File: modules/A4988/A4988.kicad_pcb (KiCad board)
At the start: 2 copper layers, 40.6 x 40.6 mm, 19 parts, among them J1 Conn_01x10_Male, J2 Conn_01x10_Male, J3 Conn_01x08_Female, J4 Conn_01x08_Female, J5 Conn_01x04_Male, J6 Conn_01x02_Female, SW1 SW_DIP_x03

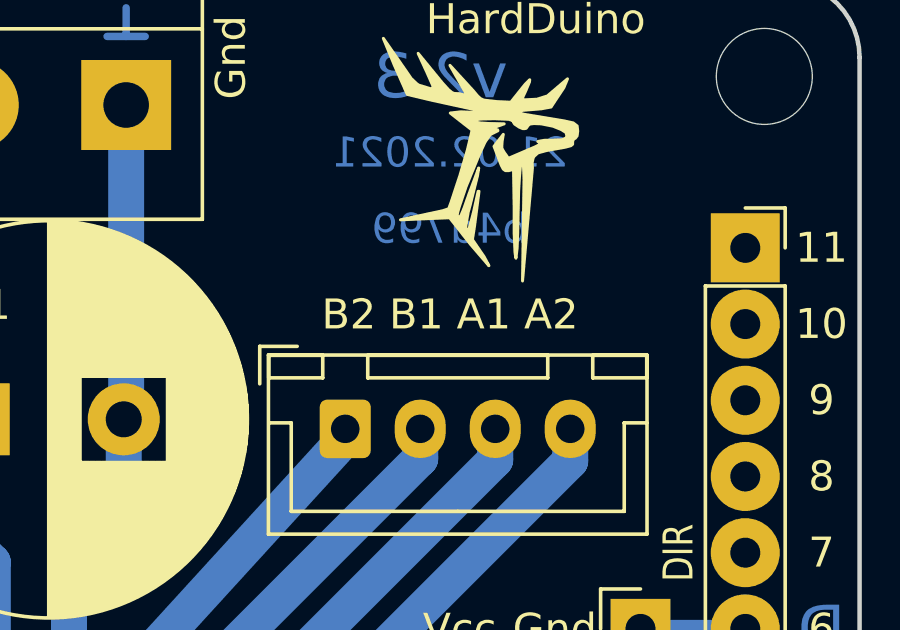
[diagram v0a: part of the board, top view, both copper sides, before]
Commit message: Rename pins. I don't know where I got old names but I found new names on A4988 pcb.
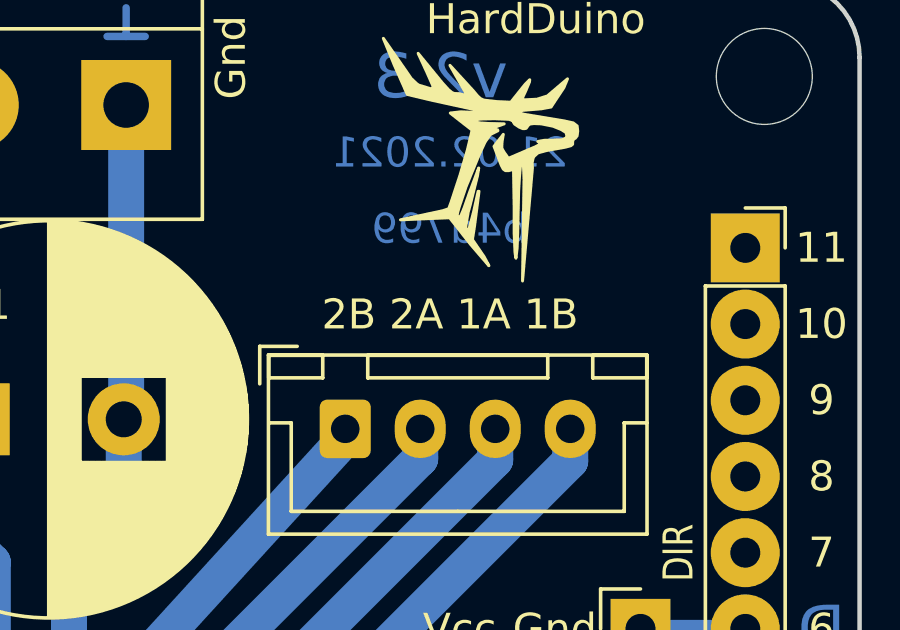
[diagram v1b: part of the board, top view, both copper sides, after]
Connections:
- net /MA1 renamed /1A
- net /MA2 renamed /1B
- net /MB1 renamed /2A
- net /MB2 renamed /2B
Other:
- board text added: "2B 2A 1A 1B"
- board text removed: "B2 B1 A1 A2"

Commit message: Fix hashes
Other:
- board text added: "23.02.2021"
- board text added: "513641"
- board text removed: "21.02.2021"
- board text removed: "b4d799"

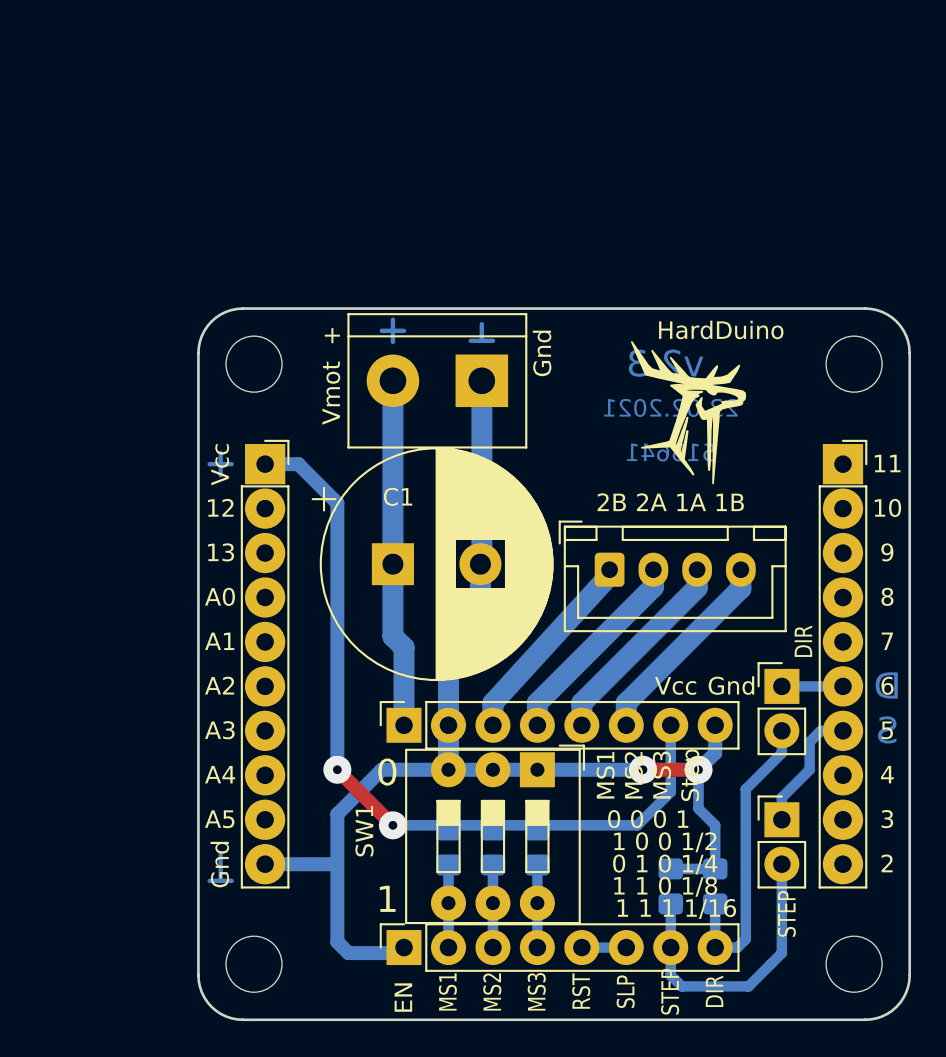
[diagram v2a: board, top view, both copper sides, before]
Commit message: Move mounting holes closer
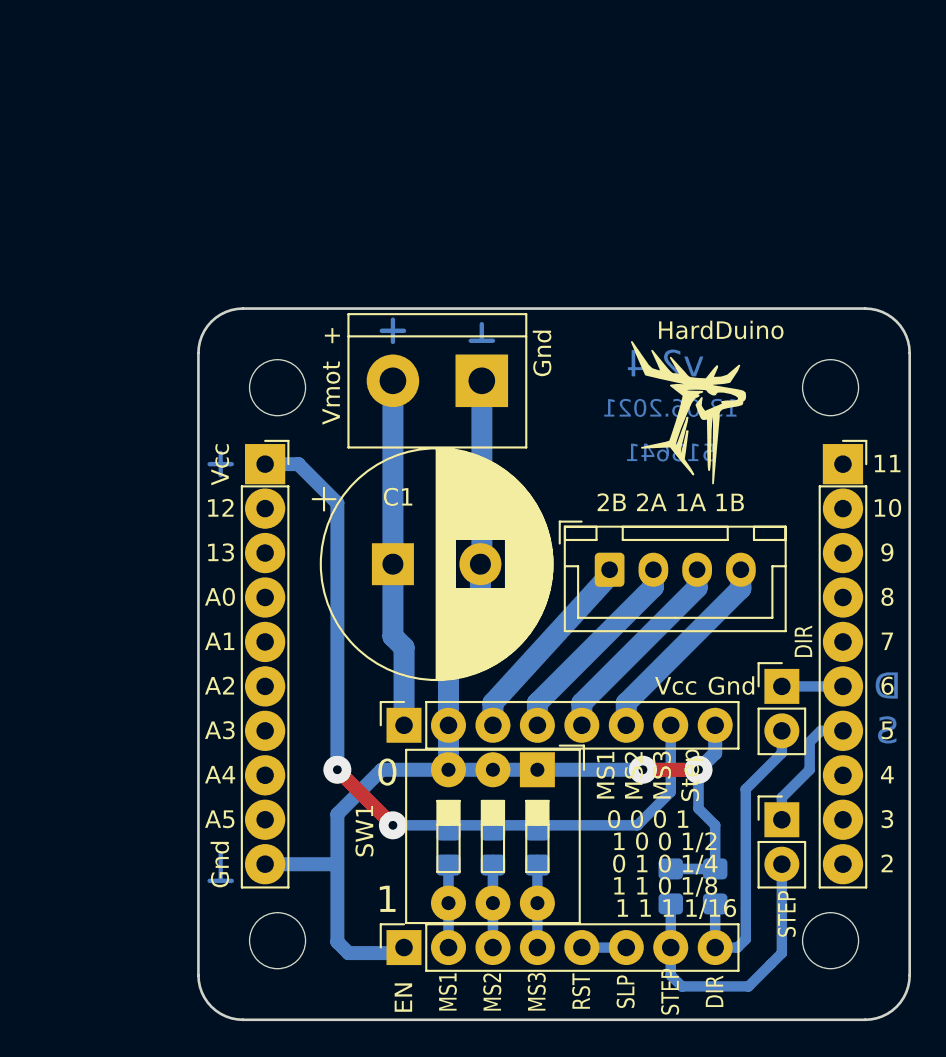
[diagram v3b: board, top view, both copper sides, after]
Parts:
- moved H1 1.90 mm to (93.4, 55.3)
- moved H2 1.90 mm to (93.4, 86.9)
- moved H3 1.90 mm to (125.0, 55.3)
- moved H4 1.90 mm to (125.0, 86.9)
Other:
- board text added: "13.06.2021"
- board text added: "v2.4"
- board text removed: "23.02.2021"
- board text removed: "v2.3"

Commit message: v2.5, size was changed to 31.1 x 31.92
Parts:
- moved H1 0.30 mm to (93.7, 55.2)
- moved H3 0.30 mm to (124.8, 55.2)
- moved H2 0.30 mm to (93.7, 87.1)
- moved H4 0.30 mm to (124.8, 87.1)
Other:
- board text added: "17.06.2021"
- board text added: "v2.5"
- board text removed: "13.06.2021"
- board text removed: "v2.4"

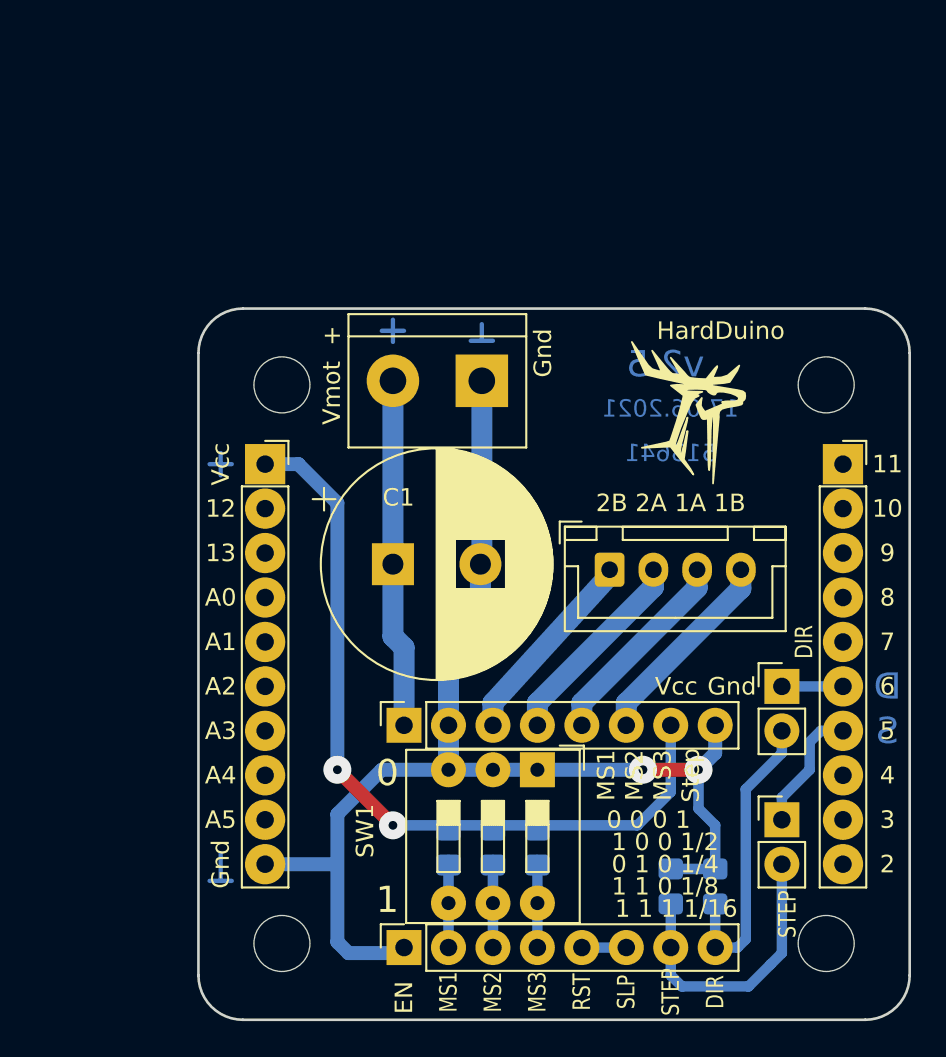
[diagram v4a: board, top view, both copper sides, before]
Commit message: All 1x shields was rotated clockwise
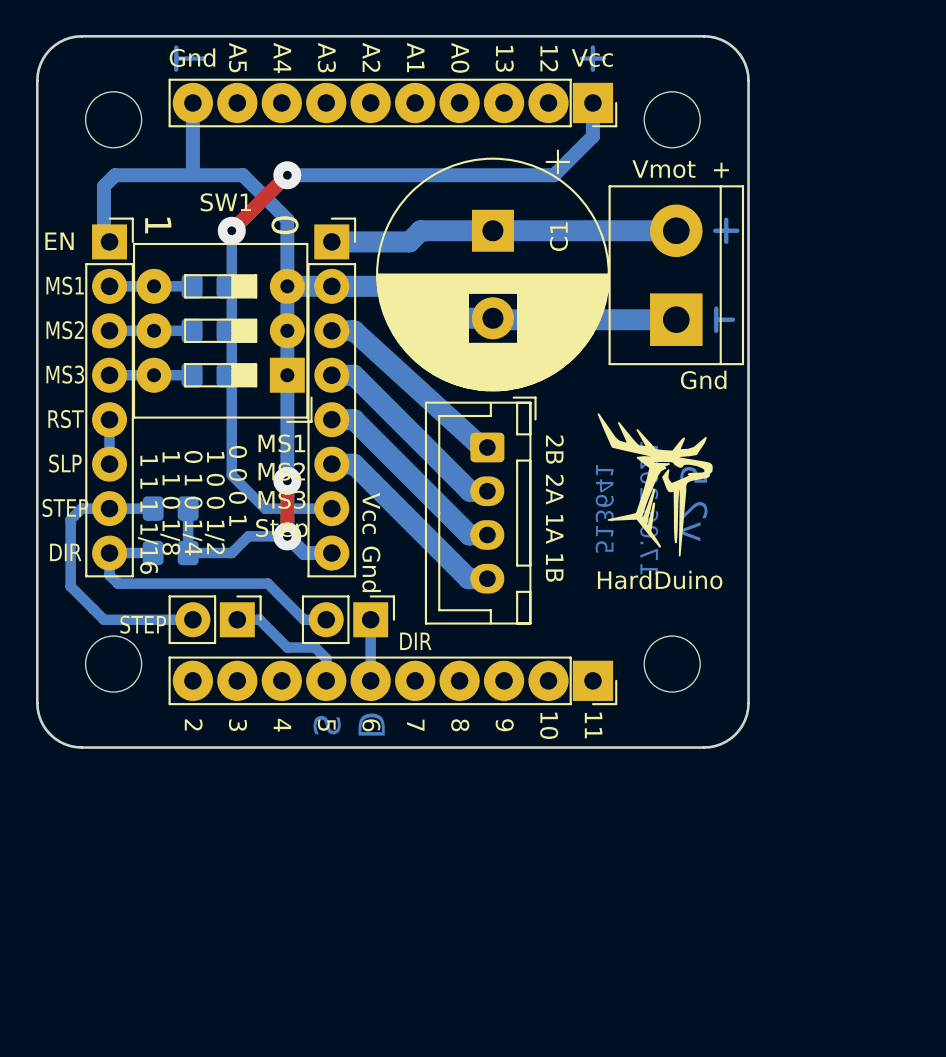
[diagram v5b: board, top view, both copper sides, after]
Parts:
- moved H2 48.0 mm to (84.1, 40.0), turned to 270 degrees
- moved H4 43.7 mm to (84.1, 71.1), turned to 270 degrees
- moved J3 43.7 mm to (83.8, 47.0), turned to 0 degrees
- moved R5 36.5 mm to (87.3, 64.8), turned to 0 degrees
- moved R4 35.8 mm to (87.3, 62.2), turned to 0 degrees
- moved R1 34.9 mm to (89.5, 49.5), turned to 180 degrees
- moved R2 33.7 mm to (89.5, 52.1), turned to 180 degrees
- moved JP1 33.1 mm to (91.1, 68.6), turned to 270 degrees
- moved R3 32.9 mm to (89.5, 54.6), turned to 180 degrees
- moved J4 27.9 mm to (96.5, 47.0), turned to 0 degrees
- moved J1 27.9 mm to (111.4, 39.1), turned to 270 degrees
- moved H1 27.0 mm to (116.0, 40.0), turned to 270 degrees
- moved SW1 26.7 mm to (94.0, 54.6), turned to 180 degrees
- moved JP2 23.8 mm to (98.7, 68.6), turned to 270 degrees
- moved C1 19.9 mm to (105.7, 46.4), turned to 270 degrees
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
